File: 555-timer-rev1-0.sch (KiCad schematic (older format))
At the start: 19 parts, among them J1 Conn_01x02_Female, SW1 SW_Push, SW2 SW_Push, U1 SA555D

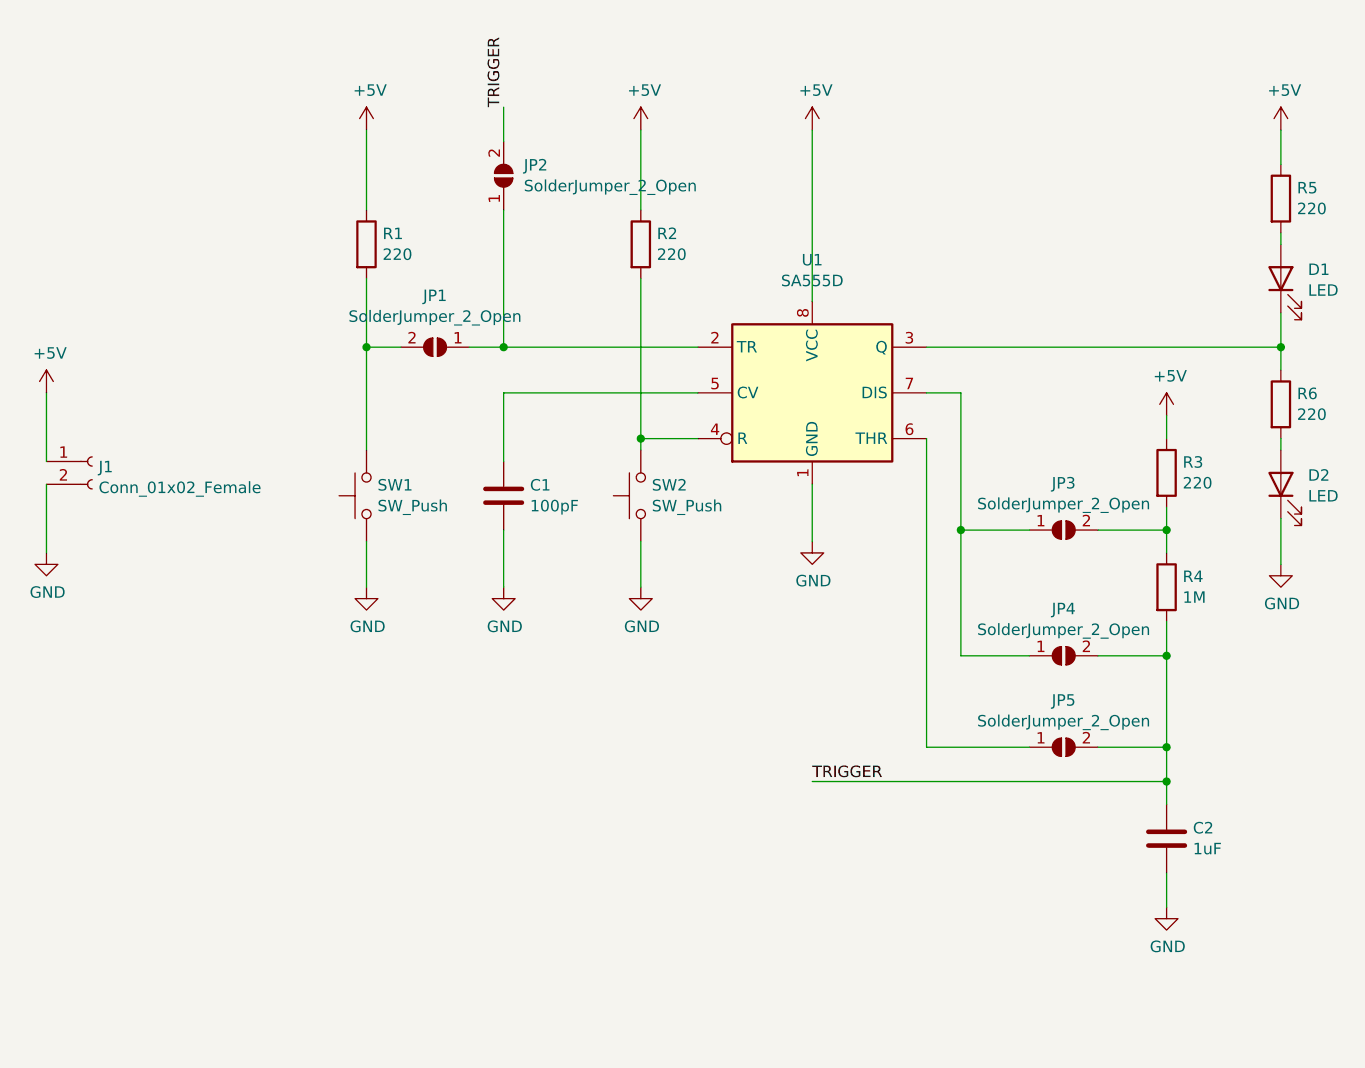
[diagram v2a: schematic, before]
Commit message: Create and assign layout for switches.
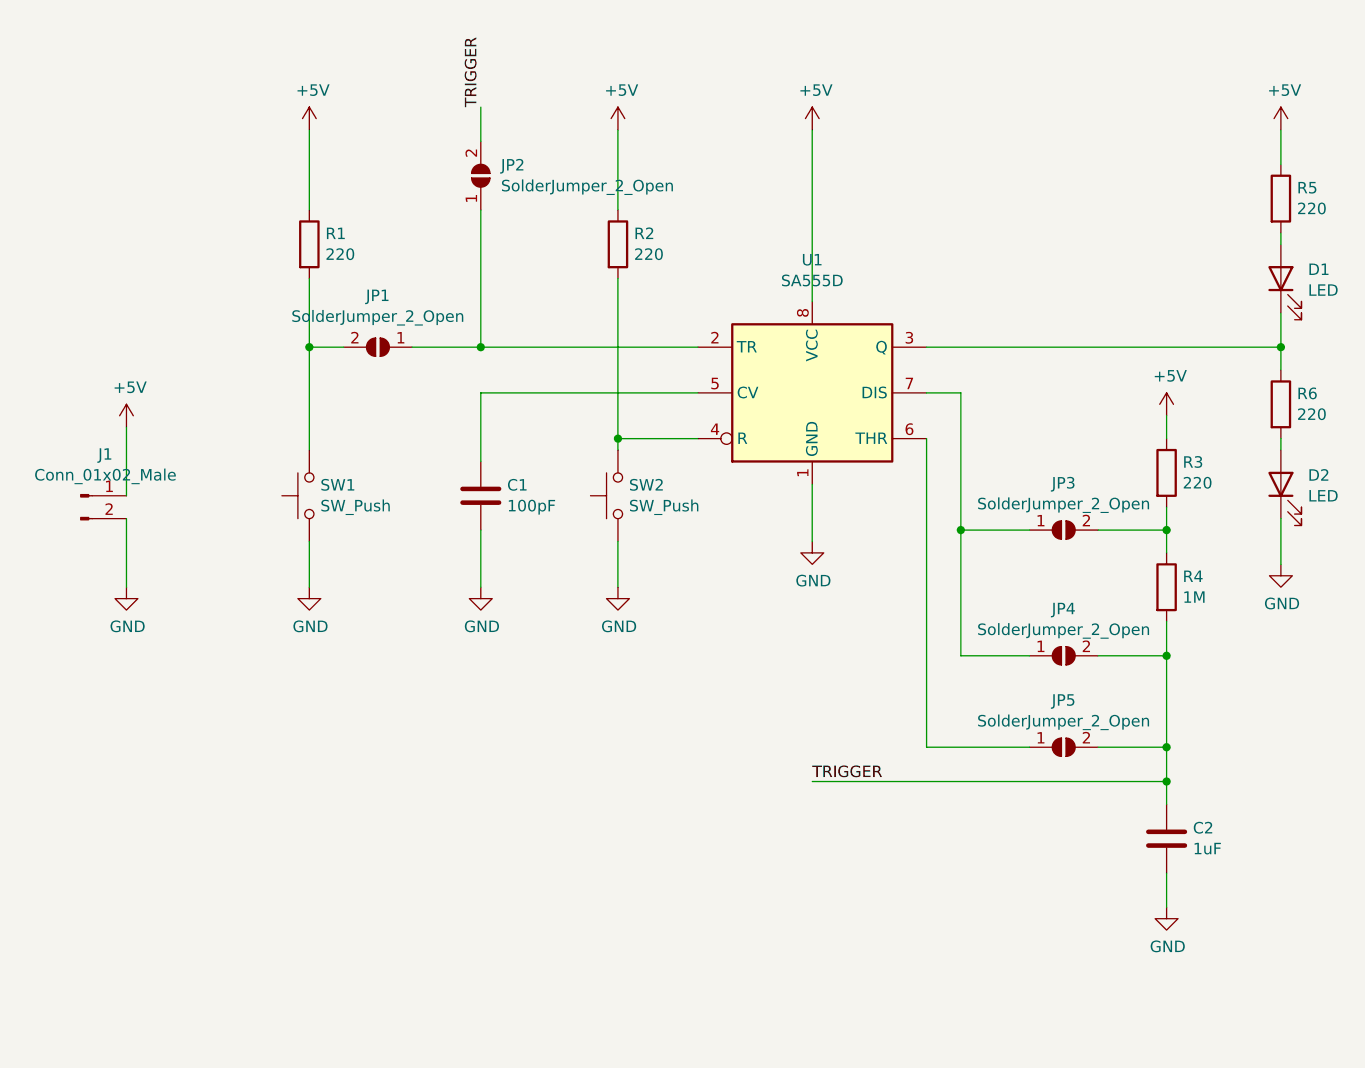
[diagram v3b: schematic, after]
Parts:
- removed J1: Conn_01x02_Female, Connector_PinSocket_2.54mm:PinSocket_1x02_P2.54mm_Vertical, symbol 555-timer-rev1-0:Conn_01x02_Female
- added J1: Conn_01x02_Male, Connector_PinHeader_2.54mm:PinHeader_1x02_P2.54mm_Vertical, symbol Connector:Conn_01x02_Male
- SW1, SW2: footprint (none) -> electronics-555-timer-rev1-0:SW_SPST_PTS647
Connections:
- net +5V: now also J1.1 (Pin_1)
- net GND: now also J1.2 (Pin_2)
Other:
- moved on the sheet: C1, JP1, JP2, R1, R2
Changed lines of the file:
@@
 L Device:C C1
 U 1 1 5F27D81E
-P 4650 4450
-F 0 "C1" H 4765 4496 50  0000 L CNN
-F 1 "100pF" H 4765 4405 50  0000 L CNN
-F 2 "Capacitor_SMD:C_1206_3216Metric_Pad1.42x1.75mm_HandSolder" H 4688 4300 50  0001 C CNN
-F 3 "~" H 4650 4450 50  0001 C CNN
-	1    4650 4450
+P 4550 4450
+F 0 "C1" H 4665 4496 50  0000 L CNN
+F 1 "100pF" H 4665 4405 50  0000 L CNN
+F 2 "Capacitor_SMD:C_1206_3216Metric_Pad1.42x1.75mm_HandSolder" H 4588 4300 50  0001 C CNN
+F 3 "~" H 4550 4450 50  0001 C CNN
+	1    4550 4450
 	1    0    0    -1
 $EndComp
@@
 Wire Wire Line
 	6500 4000 6650 4000
-$Comp
-L 555-timer-rev1-0:Conn_01x02_Female J1
-U 1 1 5F292F1E
-P 2850 4300
-F 0 "J1" H 2878 4276 50  0000 L CNN
-F 1 "Conn_01x02_Female" H 2878 4185 50  0000 L CNN
-F 2 "Connector_PinSocket_2.54mm:PinSocket_1x02_P2.54mm_Vertical" H 2850 4300 50  0001 C CNN
-F 3 "~" H 2850 4300 50  0001 C CNN
-	1    2850 4300
-	1    0    0    -1
-$EndComp
 Wire Wire Line
 	8050 3300 8050 3350
@@
 L power:+5V #PWR01
 U 1 1 5F2B0EB0
-P 2650 4000
-F 0 "#PWR01" H 2650 3850 50  0001 C CNN
-F 1 "+5V" H 2665 4173 50  0000 C CNN
-F 2 "" H 2650 4000 50  0001 C CNN
-F 3 "" H 2650 4000 50  0001 C CNN
-	1    2650 4000
+P 3000 4150
+F 0 "#PWR01" H 3000 4000 50  0001 C CNN
+F 1 "+5V" H 3015 4323 50  0000 C CNN
+F 2 "" H 3000 4150 50  0001 C CNN
+F 3 "" H 3000 4150 50  0001 C CNN
+	1    3000 4150
 	1    0    0    -1
 $EndComp
@@
 L power:GND #PWR02
 U 1 1 5F2B1695
-P 2650 4700
-F 0 "#PWR02" H 2650 4450 50  0001 C CNN
-F 1 "GND" H 2655 4527 50  0000 C CNN
-F 2 "" H 2650 4700 50  0001 C CNN
-F 3 "" H 2650 4700 50  0001 C CNN
-	1    2650 4700
-	1    0    0    -1
-$EndComp
-Wire Wire Line
-	2650 4400 2650 4700
-Wire Wire Line
-	2650 4300 2650 4000
+P 3000 4850
+F 0 "#PWR02" H 3000 4600 50  0001 C CNN
+F 1 "GND" H 3005 4677 50  0000 C CNN
+F 2 "" H 3000 4850 50  0001 C CNN
+F 3 "" H 3000 4850 50  0001 C CNN
+	1    3000 4850
+	1    0    0    -1
+$EndComp
+Wire Wire Line
+	3000 4550 3000 4850
+Wire Wire Line
+	3000 4450 3000 4150
 $Comp
 L power:+5V #PWR08
@@
 L power:GND #PWR05
 U 1 1 5F2B3448
-P 4650 4850
-F 0 "#PWR05" H 4650 4600 50  0001 C CNN
-F 1 "GND" H 4655 4677 50  0000 C CNN
-F 2 "" H 4650 4850 50  0001 C CNN
-F 3 "" H 4650 4850 50  0001 C CNN
-	1    4650 4850
-	1    0    0    -1
-$EndComp
-Wire Wire Line
-	4650 4600 4650 4850
+P 4550 4850
+F 0 "#PWR05" H 4550 4600 50  0001 C CNN
+F 1 "GND" H 4555 4677 50  0000 C CNN
+F 2 "" H 4550 4850 50  0001 C CNN
+F 3 "" H 4550 4850 50  0001 C CNN
+	1    4550 4850
+	1    0    0    -1
+$EndComp
+Wire Wire Line
+	4550 4600 4550 4850
 Wire Wire Line
 	7550 4500 7550 4600
@@
 	6500 4200 6500 5550
 Wire Wire Line
-	4650 4000 4650 4300
+	4550 4000 4550 4300
 Wire Wire Line
 	8050 3650 8050 3800
@@
 Wire Wire Line
 	8050 3800 8050 3900
-Text Label 4650 2750 1    50   ~ 0
-TRIGGER
 Text Label 6000 5700 0    50   ~ 0
 TRIGGER
@@
 L power:+5V #PWR06
 U 1 1 5F2CD6A0
-P 5250 2850
-F 0 "#PWR06" H 5250 2700 50  0001 C CNN
-F 1 "+5V" H 5265 3023 50  0000 C CNN
-F 2 "" H 5250 2850 50  0001 C CNN
-F 3 "" H 5250 2850 50  0001 C CNN
-	1    5250 2850
-	1    0    0    -1
-$EndComp
-Connection ~ 5250 4200
+P 5150 2850
+F 0 "#PWR06" H 5150 2700 50  0001 C CNN
+F 1 "+5V" H 5165 3023 50  0000 C CNN
+F 2 "" H 5150 2850 50  0001 C CNN
+F 3 "" H 5150 2850 50  0001 C CNN
+	1    5150 2850
+	1    0    0    -1
+$EndComp
+Connection ~ 5150 4200
 $Comp
 L Device:R R2
 U 1 1 5F2D3863
-P 5250 3350
-F 0 "R2" H 5320 3396 50  0000 L CNN
-F 1 "220" H 5320 3305 50  0000 L CNN
-F 2 "Resistor_SMD:R_1206_3216Metric_Pad1.42x1.75mm_HandSolder" V 5180 3350 50  0001 C CNN
-F 3 "~" H 5250 3350 50  0001 C CNN
-	1    5250 3350
-	1    0    0    -1
-$EndComp
-Wire Wire Line
-	5250 3500 5250 4200
-Wire Wire Line
-	5250 4200 5500 4200
-Wire Wire Line
-	4650 4000 5500 4000
-$Comp
-L Switch:SW_Push SW2
-U 1 1 5F2D850F
-P 5250 4450
-F 0 "SW2" V 5296 4402 50  0000 R CNN
-F 1 "SW_Push" V 5205 4402 50  0000 R CNN
-F 2 "" H 5250 4650 50  0001 C CNN
-F 3 "~" H 5250 4650 50  0001 C CNN
-	1    5250 4450
-	0    -1   -1   0
-$EndComp
+P 5150 3350
+F 0 "R2" H 5220 3396 50  0000 L CNN
+F 1 "220" H 5220 3305 50  0000 L CNN
+F 2 "Resistor_SMD:R_1206_3216Metric_Pad1.42x1.75mm_HandSolder" V 5080 3350 50  0001 C CNN
+F 3 "~" H 5150 3350 50  0001 C CNN
+	1    5150 3350
+	1    0    0    -1
+$EndComp
+Wire Wire Line
+	5150 3500 5150 4200
 $Comp
 L power:GND #PWR07
 U 1 1 5F2D9CE9
-P 5250 4850
-F 0 "#PWR07" H 5250 4600 50  0001 C CNN
-F 1 "GND" H 5255 4677 50  0000 C CNN
-F 2 "" H 5250 4850 50  0001 C CNN
-F 3 "" H 5250 4850 50  0001 C CNN
-	1    5250 4850
-	1    0    0    -1
-$EndComp
-Wire Wire Line
-	5250 4650 5250 4850
+P 5150 4850
+F 0 "#PWR07" H 5150 4600 50  0001 C CNN
+F 1 "GND" H 5155 4677 50  0000 C CNN
+F 2 "" H 5150 4850 50  0001 C CNN
+F 3 "" H 5150 4850 50  0001 C CNN
+	1    5150 4850
+	1    0    0    -1
+$EndComp
+Wire Wire Line
+	5150 4650 5150 4850
 Wire Wire Line
 	8050 2850 8050 3000
@@
 	6000 2850 6000 3600
 Wire Wire Line
-	5250 2850 5250 3200
+	5150 2850 5150 3200
 $Comp
 L power:+5V #PWR03
 U 1 1 5F2E0D58
-P 4050 2850
-F 0 "#PWR03" H 4050 2700 50  0001 C CNN
-F 1 "+5V" H 4065 3023 50  0000 C CNN
-F 2 "" H 4050 2850 50  0001 C CNN
-F 3 "" H 4050 2850 50  0001 C CNN
-	1    4050 2850
+P 3800 2850
+F 0 "#PWR03" H 3800 2700 50  0001 C CNN
+F 1 "+5V" H 3815 3023 50  0000 C CNN
+F 2 "" H 3800 2850 50  0001 C CNN
+F 3 "" H 3800 2850 50  0001 C CNN
+	1    3800 2850
 	1    0    0    -1
 $EndComp
@@
 L Device:R R1
 U 1 1 5F2E1BC2
-P 4050 3350
-F 0 "R1" H 4120 3396 50  0000 L CNN
-F 1 "220" H 4120 3305 50  0000 L CNN
-F 2 "Resistor_SMD:R_1206_3216Metric_Pad1.42x1.75mm_HandSolder" V 3980 3350 50  0001 C CNN
-F 3 "~" H 4050 3350 50  0001 C CNN
-	1    4050 3350
-	1    0    0    -1
-$EndComp
-$Comp
-L Switch:SW_Push SW1
-U 1 1 5F2E2AA0
-P 4050 4450
-F 0 "SW1" V 4096 4402 50  0000 R CNN
-F 1 "SW_Push" V 4005 4402 50  0000 R CNN
-F 2 "" H 4050 4650 50  0001 C CNN
-F 3 "~" H 4050 4650 50  0001 C CNN
-	1    4050 4450
-	0    -1   -1   0
+P 3800 3350
+F 0 "R1" H 3870 3396 50  0000 L CNN
+F 1 "220" H 3870 3305 50  0000 L CNN
+F 2 "Resistor_SMD:R_1206_3216Metric_Pad1.42x1.75mm_HandSolder" V 3730 3350 50  0001 C CNN
+F 3 "~" H 3800 3350 50  0001 C CNN
+	1    3800 3350
+	1    0    0    -1
 $EndComp
 $Comp
 L power:GND #PWR04
 U 1 1 5F2E3197
-P 4050 4850
-F 0 "#PWR04" H 4050 4600 50  0001 C CNN
-F 1 "GND" H 4055 4677 50  0000 C CNN
-F 2 "" H 4050 4850 50  0001 C CNN
-F 3 "" H 4050 4850 50  0001 C CNN
-	1    4050 4850
-	1    0    0    -1
-$EndComp
-Wire Wire Line
-	4050 2850 4050 3200
-Wire Wire Line
-	4050 3500 4050 3800
-Wire Wire Line
-	4050 4650 4050 4850
+P 3800 4850
+F 0 "#PWR04" H 3800 4600 50  0001 C CNN
+F 1 "GND" H 3805 4677 50  0000 C CNN
+F 2 "" H 3800 4850 50  0001 C CNN
+F 3 "" H 3800 4850 50  0001 C CNN
+	1    3800 4850
+	1    0    0    -1
+$EndComp
+Wire Wire Line
+	3800 2850 3800 3200
+Wire Wire Line
+	3800 3500 3800 3800
+Wire Wire Line
+	3800 4650 3800 4850
 $Comp
 L Jumper:SolderJumper_2_Open JP1
 U 1 1 5F2E496D
-P 4350 3800
-F 0 "JP1" H 4350 3575 50  0000 C CNN
-F 1 "SolderJumper_2_Open" H 4350 3666 50  0000 C CNN
-F 2 "Jumper:SolderJumper-2_P1.3mm_Open_TrianglePad1.0x1.5mm" H 4350 3800 50  0001 C CNN
-F 3 "~" H 4350 3800 50  0001 C CNN
-	1    4350 3800
+P 4100 3800
+F 0 "JP1" H 4100 3575 50  0000 C CNN
+F 1 "SolderJumper_2_Open" H 4100 3666 50  0000 C CNN
+F 2 "Jumper:SolderJumper-2_P1.3mm_Open_TrianglePad1.0x1.5mm" H 4100 3800 50  0001 C CNN
+F 3 "~" H 4100 3800 50  0001 C CNN
+	1    4100 3800
 	-1   0    0    1
 $EndComp
 Wire Wire Line
-	4500 3800 4650 3800
-Wire Wire Line
-	4200 3800 4050 3800
-Connection ~ 4050 3800
-Wire Wire Line
-	4650 3800 4650 3200
-Connection ~ 4650 3800
-Wire Wire Line
-	4650 3800 5500 3800
-$Comp
-L Jumper:SolderJumper_2_Open JP2
-U 1 1 5F2E91E4
-P 4650 3050
-F 0 "JP2" V 4696 2962 50  0000 R CNN
-F 1 "SolderJumper_2_Open" V 4605 2962 50  0000 R CNN
-F 2 "Jumper:SolderJumper-2_P1.3mm_Open_TrianglePad1.0x1.5mm" H 4650 3050 50  0001 C CNN
-F 3 "~" H 4650 3050 50  0001 C CNN
-	1    4650 3050
-	0    -1   -1   0
-$EndComp
-Wire Wire Line
-	4650 2900 4650 2750
-Wire Wire Line
-	4050 3800 4050 4250
-Wire Wire Line
-	5250 4200 5250 4250
+	3950 3800 3800 3800
+Connection ~ 3800 3800
+Wire Wire Line
+	3800 3800 3800 4250
+Wire Wire Line
+	5150 4200 5150 4250
 Wire Wire Line
 	7550 5550 7550 5700
@@
 Wire Wire Line
 	7250 5550 7550 5550
+$Comp
+L Connector:Conn_01x02_Male J1
+U 1 1 5F2FB705
+P 2800 4450
+F 0 "J1" H 2908 4631 50  0000 C CNN
+F 1 "Conn_01x02_Male" H 2908 4540 50  0000 C CNN
+F 2 "Connector_PinHeader_2.54mm:PinHeader_1x02_P2.54mm_Vertical" H 2800 4450 50  0001 C CNN
+F 3 "~" H 2800 4450 50  0001 C CNN
+	1    2800 4450
+	1    0    0    -1
+$EndComp
+Wire Wire Line
+	5150 4200 5500 4200
+Wire Wire Line
+	4250 3800 4550 3800
+Text Label 4550 2750 1    50   ~ 0
+TRIGGER
+Wire Wire Line
+	4550 3800 4550 3200
+$Comp
+L Jumper:SolderJumper_2_Open JP2
+U 1 1 5F2E91E4
+P 4550 3050
+F 0 "JP2" V 4596 2962 50  0000 R CNN
+F 1 "SolderJumper_2_Open" V 4505 2962 50  0000 R CNN
+F 2 "Jumper:SolderJumper-2_P1.3mm_Open_TrianglePad1.0x1.5mm" H 4550 3050 50  0001 C CNN
+F 3 "~" H 4550 3050 50  0001 C CNN
+	1    4550 3050
+	0    -1   -1   0
+$EndComp
+Wire Wire Line
+	4550 2900 4550 2750
+$Comp
+L Switch:SW_Push SW1
+U 1 1 5F320086
+P 3800 4450
+F 0 "SW1" V 3846 4402 50  0000 R CNN
+F 1 "SW_Push" V 3755 4402 50  0000 R CNN
+F 2 "electronics-555-timer-rev1-0:SW_SPST_PTS647" H 3800 4650 50  0001 C CNN
+F 3 "~" H 3800 4650 50  0001 C CNN
+	1    3800 4450
+	0    -1   -1   0
+$EndComp
+Wire Wire Line
+	4550 4000 5500 4000
+$Comp
+L Switch:SW_Push SW2
+U 1 1 5F3230DA
+P 5150 4450
+F 0 "SW2" V 5196 4402 50  0000 R CNN
+F 1 "SW_Push" V 5105 4402 50  0000 R CNN
+F 2 "electronics-555-timer-rev1-0:SW_SPST_PTS647" H 5150 4650 50  0001 C CNN
+F 3 "~" H 5150 4650 50  0001 C CNN
+	1    5150 4450
+	0    -1   -1   0
+$EndComp
+Wire Wire Line
+	4550 3800 5500 3800
+Connection ~ 4550 3800
 $EndSCHEMATC

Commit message: Finish PCB layout.
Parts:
- renumbered JP3 to JP2, JP4 to JP3, JP5 to JP4, JP2 to JP5
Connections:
- net +5V: now also R1.2, R5.2; no longer R1.1, R5.1
- net TRIGGER: now also JP1.2 (B), JP5.1 (A), U1.2 (TR); no longer C2.1, JP3.2 (B), JP4.2 (B), JP5.2 (B), R4.2
- net at D1.1 (K), U1.3 (Q): now also R6.2; no longer R6.1
- net at D1.2 (A): now also R5.1; no longer R5.2
- net at D2.2 (A): now also R6.1; no longer R6.2
- new net: C2.1, JP3.2 (B), JP4.2 (B), JP5.2 (B), R4.2
- new net: JP1.1 (A), R1.1, SW1.2
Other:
- moved on the sheet: JP4, JP5
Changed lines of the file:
@@
 F 3 "~" H 8050 3150 50  0001 C CNN
 	1    8050 3150
-	1    0    0    -1
+	-1   0    0    1
 $EndComp
 $Comp
@@
 F 3 "~" H 8050 4050 50  0001 C CNN
 	1    8050 4050
-	1    0    0    -1
+	-1   0    0    1
 $EndComp
 $Comp
@@
 Wire Wire Line
 	7550 4500 7550 4600
-Wire Wire Line
-	7550 5000 7550 5150
 Connection ~ 7550 4600
 Wire Wire Line
 	7550 4600 7550 4700
-Connection ~ 7550 5550
+Connection ~ 7550 5450
 $Comp
 L power:GND #PWR011
@@
 	6650 4000 6650 4600
 Wire Wire Line
-	6500 4200 6500 5550
-Wire Wire Line
 	4550 4000 4550 4300
 Wire Wire Line
@@
 Wire Wire Line
 	8050 3800 8050 3900
-Text Label 6000 5700 0    50   ~ 0
+Text Label 6000 5750 0    50   ~ 0
 TRIGGER
 $Comp
@@
 F 3 "~" H 3800 3350 50  0001 C CNN
 	1    3800 3350
-	1    0    0    -1
+	-1   0    0    1
 $EndComp
 $Comp
@@
 F 3 "~" H 4100 3800 50  0001 C CNN
 	1    4100 3800
-	-1   0    0    1
+	1    0    0    -1
 $EndComp
 Wire Wire Line
@@
 Wire Wire Line
 	5150 4200 5150 4250
-Wire Wire Line
-	7550 5550 7550 5700
-Connection ~ 7550 5700
 Wire Wire Line
 	6650 4600 6650 5150
 Connection ~ 6650 4600
 Connection ~ 7550 5150
-Wire Wire Line
-	7550 5150 7550 5550
-$Comp
-L Jumper:SolderJumper_2_Open JP3
+$Comp
+L Jumper:SolderJumper_2_Open JP2
 U 1 1 5F2FC22B
 P 7100 4600
-F 0 "JP3" H 7100 4805 50  0000 C CNN
+F 0 "JP2" H 7100 4805 50  0000 C CNN
 F 1 "SolderJumper_2_Open" H 7100 4714 50  0000 C CNN
 F 2 "Jumper:SolderJumper-2_P1.3mm_Open_TrianglePad1.0x1.5mm" H 7100 4600 50  0001 C CNN
@@
 	7250 4600 7550 4600
 $Comp
-L Jumper:SolderJumper_2_Open JP4
+L Jumper:SolderJumper_2_Open JP3
 U 1 1 5F2FCB39
 P 7100 5150
-F 0 "JP4" H 7100 5355 50  0000 C CNN
+F 0 "JP3" H 7100 5355 50  0000 C CNN
 F 1 "SolderJumper_2_Open" H 7100 5264 50  0000 C CNN
 F 2 "Jumper:SolderJumper-2_P1.3mm_Open_TrianglePad1.0x1.5mm" H 7100 5150 50  0001 C CNN
@@
 	6500 3800 8050 3800
 Wire Wire Line
-	6000 5700 7550 5700
-Wire Wire Line
-	6500 5550 6950 5550
+	6000 5750 6950 5750
+Wire Wire Line
+	6500 5450 6950 5450
 Wire Wire Line
 	6650 5150 6950 5150
@@
 	6650 4600 6950 4600
 Wire Wire Line
-	7550 5700 7550 5800
+	7550 5750 7550 5800
 Wire Wire Line
 	7550 6100 7550 6250
 $Comp
-L Jumper:SolderJumper_2_Open JP5
+L Jumper:SolderJumper_2_Open JP4
 U 1 1 5F3182F6
-P 7100 5550
-F 0 "JP5" H 7100 5755 50  0000 C CNN
-F 1 "SolderJumper_2_Open" H 7100 5664 50  0000 C CNN
-F 2 "Jumper:SolderJumper-2_P1.3mm_Open_TrianglePad1.0x1.5mm" H 7100 5550 50  0001 C CNN
-F 3 "~" H 7100 5550 50  0001 C CNN
-	1    7100 5550
-	1    0    0    -1
-$EndComp
-Wire Wire Line
-	7250 5550 7550 5550
+P 7100 5450
+F 0 "JP4" H 7100 5655 50  0000 C CNN
+F 1 "SolderJumper_2_Open" H 7100 5564 50  0000 C CNN
+F 2 "Jumper:SolderJumper-2_P1.3mm_Open_TrianglePad1.0x1.5mm" H 7100 5450 50  0001 C CNN
+F 3 "~" H 7100 5450 50  0001 C CNN
+	1    7100 5450
+	1    0    0    -1
+$EndComp
+Wire Wire Line
+	7250 5450 7550 5450
 $Comp
 L Connector:Conn_01x02_Male J1
@@
 Wire Wire Line
 	4250 3800 4550 3800
-Text Label 4550 2750 1    50   ~ 0
+Text Label 4550 2950 1    50   ~ 0
 TRIGGER
-Wire Wire Line
-	4550 3800 4550 3200
-$Comp
-L Jumper:SolderJumper_2_Open JP2
+$Comp
+L Jumper:SolderJumper_2_Open JP5
 U 1 1 5F2E91E4
-P 4550 3050
-F 0 "JP2" V 4596 2962 50  0000 R CNN
-F 1 "SolderJumper_2_Open" V 4505 2962 50  0000 R CNN
-F 2 "Jumper:SolderJumper-2_P1.3mm_Open_TrianglePad1.0x1.5mm" H 4550 3050 50  0001 C CNN
-F 3 "~" H 4550 3050 50  0001 C CNN
-	1    4550 3050
-	0    -1   -1   0
-$EndComp
-Wire Wire Line
-	4550 2900 4550 2750
+P 7100 5750
+F 0 "JP5" H 7200 5900 50  0000 R CNN
+F 1 "SolderJumper_2_Open" H 7500 5850 50  0000 R CNN
+F 2 "Jumper:SolderJumper-2_P1.3mm_Open_TrianglePad1.0x1.5mm" H 7100 5750 50  0001 C CNN
+F 3 "~" H 7100 5750 50  0001 C CNN
+	1    7100 5750
+	1    0    0    -1
+$EndComp
 $Comp
 L Switch:SW_Push SW1
@@
 	4550 3800 5500 3800
 Connection ~ 4550 3800
+Wire Wire Line
+	7250 5750 7550 5750
+Wire Wire Line
+	4550 2950 4550 3800
+Wire Wire Line
+	6500 4200 6500 5450
+Wire Wire Line
+	7550 5150 7550 5450
+Wire Wire Line
+	7550 5450 7550 5750
+Wire Wire Line
+	7550 5000 7550 5150
+Connection ~ 7550 5750
 $EndSCHEMATC
